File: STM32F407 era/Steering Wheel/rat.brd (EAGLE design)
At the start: 99.2 x 116.2 mm, 117 parts, among them IC1 REG1117, IC3 PCA82C250T, Q1 8 MHz, U2 MAX6817EUT+T, U3 MAX6817EUT+T, U4 MAX6817EUT+T, X1 MINI-USB-SCHIELD-32005-201

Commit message: minor changes
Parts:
- X1: value MINI-USB-SCHIELD-32005-201 -> (none)
- moved C1 5.13 mm to (249.7, -1.29), turned to 90 degrees
- moved Q1 0.95 mm to (249.7, 6.39)
- moved C2 0.88 mm to (249.7, 14.1), turned to 270 degrees
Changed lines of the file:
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@@
 <setting verticaltext="up"/>
 </settings>
-<grid distance="0.0125" unitdist="inch" unit="inch" style="lines" multiple="1" display="yes" altdistance="0.025" altunitdist="inch" altunit="inch"/>
+<grid distance="0.00125" unitdist="inch" unit="inch" style="lines" multiple="1" display="yes" altdistance="0.025" altunitdist="inch" altunit="inch"/>
 <layers>
 <layer number="1" name="Top" color="4" fill="1" visible="yes" active="yes"/>
@@
 </autorouter>
 <elements>
-<element name="Q1" library="crystal" package="HC49U70" value="8 MHz" x="249.659596875" y="7.3434375" rot="R270">
-<attribute name="OC_NEWARK" value="unknown" x="249.659596875" y="7.3434375" size="1.778" layer="27" rot="R270" display="off"/>
-<attribute name="MPN" value="" x="249.659596875" y="7.3434375" size="1.778" layer="27" rot="R270" display="off"/>
-<attribute name="MF" value="" x="249.659596875" y="7.3434375" size="1.778" layer="27" rot="R270" display="off"/>
-<attribute name="OC_FARNELL" value="unknown" x="249.659596875" y="7.3434375" size="1.778" layer="27" rot="R270" display="off"/>
+<element name="Q1" library="crystal" package="HC49U70" value="8 MHz" x="249.659596875" y="6.3909375" rot="R270">
+<attribute name="OC_NEWARK" value="unknown" x="249.659596875" y="6.3909375" size="1.778" layer="27" rot="R270" display="off"/>
+<attribute name="MPN" value="" x="249.659596875" y="6.3909375" size="1.778" layer="27" rot="R270" display="off"/>
+<attribute name="MF" value="" x="249.659596875" y="6.3909375" size="1.778" layer="27" rot="R270" display="off"/>
+<attribute name="OC_FARNELL" value="unknown" x="249.659596875" y="6.3909375" size="1.778" layer="27" rot="R270" display="off"/>
 </element>
 <element name="IC3" library="micro-philips" package="SO8" value="PCA82C250T" x="196.56425" y="20.574" rot="R90">
@@
 <element name="8-BIT-DIP" library="smd-special" package="SMS-008" value="SWS008" x="241.935" y="-13.335" rot="MR0"/>
 <element name="U$5" library="red_segment" package="BIGSEVENSEGMENT" value="BIGSEVENSEGMENT" x="221.615" y="53.975"/>
-<element name="C1" library="rcl" package="C0603K" value="22pf" x="245.535709375" y="1.763078125"/>
-<element name="C2" library="rcl" package="C0603K" value="22pf" x="248.793671875" y="14.207171875"/>
+<element name="C1" library="rcl" package="C0603K" value="22pf" x="249.665171875" y="-1.288790625" rot="R90"/>
+<element name="C2" library="rcl" package="C0603K" value="22pf" x="249.665171875" y="14.064578125" rot="R270"/>
 <element name="R21" library="rcl" package="R0603" value="200" x="233.045" y="-9.2075" rot="R270"/>
 <element name="R22" library="rcl" package="R0603" value="200" x="235.585" y="-9.2075" rot="R270"/>
@@
 <element name="C24" library="microbuilder" package="_0402MP" value="1u" x="245.0465" y="9.81075"/>
 <element name="C25" library="microbuilder" package="_0402MP" value="4u7" x="245.6815" y="4.699"/>
-<element name="X1" library="con-cypressindustries" package="32005-201" value="MINI-USB-SCHIELD-32005-201" x="182.02275" y="-0.0635" rot="R15">
+<element name="X1" library="con-cypressindustries" package="32005-201" value="" x="182.02275" y="-0.0635" rot="R15">
 <attribute name="OC_NEWARK" value="unknown" x="182.02275" y="-0.0635" size="1.778" layer="27" rot="R15" display="off"/>
 <attribute name="MPN" value="" x="182.02275" y="-0.0635" size="1.778" layer="27" rot="R15" display="off"/>
@@
 <contactref element="C2" pad="2"/>
 <contactref element="U1" pad="13"/>
-<wire x1="242.89925" y1="6.57225" x2="246.475409375" y2="6.57225" width="0.3048" layer="1"/>
-<wire x1="246.475409375" y1="6.57225" x2="249.659596875" y2="9.7564375" width="0.3048" layer="1"/>
-<wire x1="249.659596875" y1="9.7564375" x2="249.668671875" y2="9.7655125" width="0.3048" layer="1"/>
-<wire x1="249.668671875" y1="9.7655125" x2="249.668671875" y2="14.207171875" width="0.3048" layer="1"/>
+<wire x1="242.89925" y1="6.57225" x2="247.427909375" y2="6.57225" width="0.3048" layer="1"/>
+<wire x1="247.427909375" y1="6.57225" x2="249.659596875" y2="8.8039375" width="0.3048" layer="1"/>
+<wire x1="249.659596875" y1="8.8039375" x2="249.665171875" y2="8.8095125" width="0.3048" layer="1"/>
+<wire x1="249.665171875" y1="8.8095125" x2="249.665171875" y2="13.189578125" width="0.3048" layer="1"/>
 </signal>
 <signal name="N$2">
@@
 <contactref element="C1" pad="2"/>
 <contactref element="U1" pad="12"/>
-<wire x1="242.89925" y1="6.07225" x2="248.517784375" y2="6.07225" width="0.3048" layer="1"/>
-<wire x1="248.517784375" y1="6.07225" x2="249.659596875" y2="4.9304375" width="0.3048" layer="1"/>
-<wire x1="249.659596875" y1="4.9304375" x2="249.649209375" y2="4.92005" width="0.3048" layer="1"/>
-<wire x1="246.410709375" y1="1.763078125" x2="246.8097375" y2="2.080578125" width="0.3048" layer="1"/>
-<wire x1="246.8097375" y1="2.080578125" x2="249.659596875" y2="4.9304375" width="0.3048" layer="1"/>
+<wire x1="242.89925" y1="6.07225" x2="247.565284375" y2="6.07225" width="0.3048" layer="1"/>
+<wire x1="247.565284375" y1="6.07225" x2="249.659596875" y2="3.9779375" width="0.3048" layer="1"/>
+<wire x1="249.659596875" y1="3.9779375" x2="249.665171875" y2="3.9723625" width="0.3048" layer="1"/>
+<wire x1="249.665171875" y1="3.9723625" x2="249.665171875" y2="-0.413790625" width="0.3048" layer="1"/>
 </signal>
 <signal name="N$51">
@@
 <wire x1="225.17825" y1="1.07225" x2="225.171" y2="1.0795" width="0.3048" layer="1"/>
 <wire x1="225.171" y1="1.0795" x2="225.171" y2="1.651" width="0.3048" layer="1"/>
-<wire x1="248.832" y1="-2.46925" x2="248.82475" y2="-2.4765" width="0.3048" layer="1"/>
 <wire x1="242.89925" y1="10.07225" x2="242.89925" y2="10.06475" width="0.3048" layer="1"/>
 <wire x1="242.89925" y1="10.06475" x2="241.45875" y2="10.06475" width="0.3048" layer="1"/>
@@
 <wire x1="242.89925" y1="5.07225" x2="244.37975" y2="5.07225" width="0.3048" layer="1"/>
 <wire x1="244.37975" y1="5.07225" x2="244.37975" y2="4.73075" width="0.3048" layer="1"/>
-<wire x1="240.79925" y1="14.17225" x2="240.79925" y2="15.12025" width="0.3048" layer="1"/>
-<wire x1="240.79925" y1="15.12025" x2="241.1095" y2="15.4305" width="0.3048" layer="1"/>
-<wire x1="241.1095" y1="15.4305" x2="241.3635" y2="15.4305" width="0.3048" layer="1"/>
-<wire x1="241.3635" y1="15.4305" x2="241.39525" y2="15.46225" width="0.3048" layer="1"/>
-<wire x1="241.39525" y1="15.46225" x2="241.39525" y2="16.16075" width="0.3048" layer="1"/>
-<wire x1="241.39525" y1="16.16075" x2="241.427" y2="16.0655" width="0.3048" layer="1"/>
 <wire x1="244.2178" y1="-14.87" x2="243.16225" y2="-14.87" width="0.3048" layer="1"/>
 <wire x1="243.16225" y1="-14.87" x2="243.078" y2="-14.95425" width="0.3048" layer="1"/>
@@
 <via x="229.39375" y="9.8425" extent="1-16" drill="0.3302"/>
 <via x="229.33025" y="11.684" extent="1-16" drill="0.3302"/>
-<via x="249.39625" y="0.762" extent="1-16" drill="0.3302"/>
+<via x="247.17375" y="-0.1905" extent="1-16" drill="0.3302"/>
 <via x="251.42825" y="13.2715" extent="1-16" drill="0.3302"/>
 <via x="239.903" y="24.28875" extent="1-16" drill="0.3302"/>
@@
 <via x="256.0955" y="23.01875" extent="1-16" drill="0.3302"/>
 <via x="256.0955" y="25.55875" extent="1-16" drill="0.3302"/>
+<wire x1="240.79925" y1="14.17225" x2="240.79925" y2="12.7245" width="0.3048" layer="1"/>
+<wire x1="240.79925" y1="12.7245" x2="241.2365" y2="12.28725" width="0.3048" layer="1"/>
 </signal>
 <signal name="TCTEMPOFF">
@@
 <contactref element="U1" pad="19"/>
 <contactref element="C10" pad="1"/>
-<wire x1="243.79275" y1="9.57225" x2="244.221" y2="9.144" width="0.3048" layer="1"/>
-<wire x1="244.221" y1="9.144" x2="244.5385" y2="9.144" width="0.3048" layer="1"/>
 <contactref element="U1" pad="28"/>
 <contactref element="C9" pad="1"/>
@@
 <wire x1="240.29925" y1="9.57225" x2="240.29925" y2="12.41425" width="0.3048" layer="1"/>
 <wire x1="242.89925" y1="9.57225" x2="240.29925" y2="9.57225" width="0.3048" layer="1"/>
-<wire x1="242.89925" y1="9.57225" x2="243.79275" y2="9.57225" width="0.3048" layer="1"/>
 <wire x1="192.024" y1="9.2075" x2="190.77175" y2="9.2075" width="0.6096" layer="1"/>
 <wire x1="190.77175" y1="9.2075" x2="190.77175" y2="12.573" width="0.6096" layer="1"/>
@@
 <wire x1="252.095" y1="-5.207" x2="254.635" y2="-5.207" width="0.3048" layer="1"/>
 <wire x1="254.635" y1="-5.207" x2="257.7465" y2="-2.0955" width="0.3048" layer="1"/>
+<wire x1="242.89925" y1="9.57225" x2="244.5385" y2="9.57225" width="0.3048" layer="1"/>
+<wire x1="244.5385" y1="9.57225" x2="244.5385" y2="9.81075" width="0.3048" layer="1"/>
 </signal>
 <signal name="12V">
@@
 <via x="229.13975" y="-2.3495" extent="1-16" drill="0.3302"/>
 <wire x1="229.13975" y1="-2.3495" x2="230.124" y2="-3.33375" width="0.3048" layer="16"/>
-<wire x1="247.68175" y1="-3.58775" x2="253.5555" y2="2.286" width="0.3048" layer="16"/>
 <via x="254.92075" y="11.65225" extent="1-16" drill="0.3302"/>
 <wire x1="254.92075" y1="11.65225" x2="257.7465" y2="11.65225" width="0.3048" layer="1"/>
@@
 <wire x1="253.5555" y1="2.286" x2="253.5555" y2="10.287" width="0.3048" layer="16"/>
 <wire x1="253.5555" y1="10.287" x2="254.92075" y2="11.65225" width="0.3048" layer="16"/>
+<wire x1="247.68175" y1="-3.58775" x2="253.5555" y2="2.286" width="0.3048" layer="16"/>
 </signal>
 <signal name="JTAG-TDO">
@@
 </signal>
 </signals>
+<errors>
+</errors>
 </board>
 </drawing>

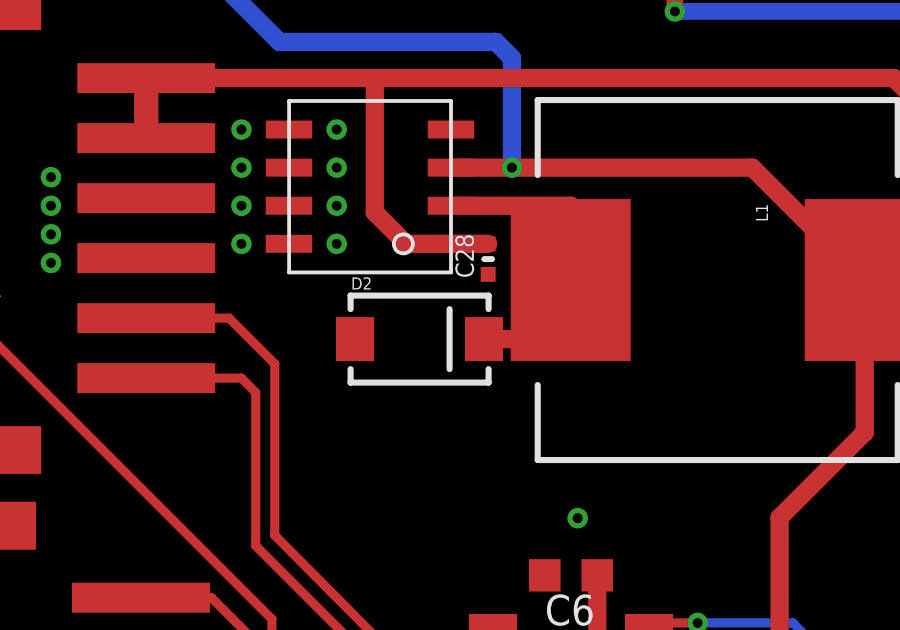
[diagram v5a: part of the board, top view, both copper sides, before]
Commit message: added bracing PCB for rotational switch
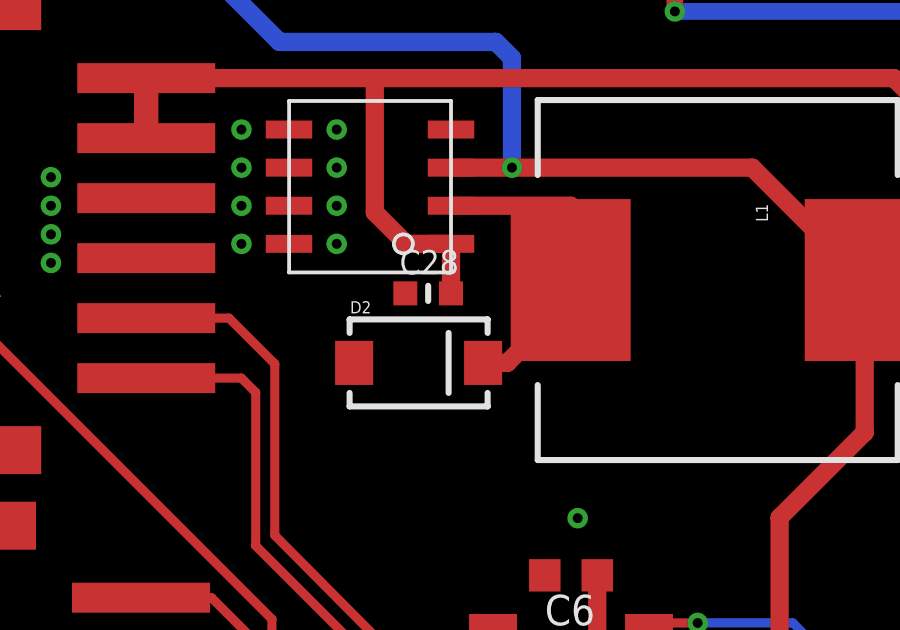
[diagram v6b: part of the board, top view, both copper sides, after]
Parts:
- C28: device microbuilder:_0402MP -> microbuilder:_0603MP
- moved C28 2.30 mm to (191.8, 33.5), turned to 0 degrees
- moved D2 0.79 mm to (191.5, 31.1)
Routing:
- net N$46: track 10.9 -> 11.8 mm
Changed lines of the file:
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@@
 <attribute name="OC_FARNELL" value="unknown" x="182.02275" y="-0.0635" size="1.778" layer="27" rot="R15" display="off"/>
 </element>
-<element name="C28" library="microbuilder" package="_0402MP" value="100n" x="193.802" y="34.6075" rot="R90"/>
+<element name="C28" library="microbuilder" package="_0603MP" value="100n" x="191.80175" y="33.4645"/>
 <element name="L1" library="SparkFun-Passives" package="CDRH125" value="MSS1038-473MLC 47u" x="201.45375" y="33.909" rot="R270"/>
-<element name="D2" library="SparkFun-DiscreteSemi" package="SMA-DIODE" value="B340A-13-F" x="191.516" y="31.9405">
-<attribute name="PROD_ID" value="DIO-08053" x="191.516" y="31.9405" size="1.778" layer="27" display="off"/>
+<element name="D2" library="SparkFun-DiscreteSemi" package="SMA-DIODE" value="B340A-13-F" x="191.48425" y="31.14675">
+<attribute name="PROD_ID" value="DIO-08053" x="191.48425" y="31.14675" size="1.778" layer="27" display="off"/>
 </element>
 <element name="C29" library="microbuilder" package="0805" value="10u" x="210.15325" y="34.0995" rot="R90"/>
@@
 <wire x1="190.02375" y1="36.16325" x2="190.02375" y2="40.64" width="0.6096" layer="1"/>
 <wire x1="182.40525" y1="38.63975" x2="182.405" y2="38.64" width="0.6096" layer="1"/>
-<wire x1="192.56375" y1="35.1155" x2="193.802" y2="35.1155" width="0.6096" layer="1"/>
+<wire x1="192.56375" y1="35.1155" x2="192.56375" y2="33.4645" width="0.6096" layer="1"/>
 <contactref element="IC1" pad="3"/>
 <wire x1="212.3186" y1="39.71925" x2="212.3186" y2="39.9796" width="0.4064" layer="1"/>
@@
 <wire x1="196.55375" y1="36.3855" x2="196.55375" y2="33.909" width="0.6096" layer="1"/>
 <contactref element="D2" pad="C"/>
-<wire x1="193.666" y1="31.9405" x2="195.86575" y2="31.9405" width="0.6096" layer="1"/>
 <wire x1="195.86575" y1="31.9405" x2="196.05625" y2="32.131" width="0.6096" layer="1"/>
-<wire x1="196.05625" y1="32.131" x2="196.05625" y2="33.4115" width="0.6096" layer="1"/>
+<wire x1="196.05625" y1="32.131" x2="196.05625" y2="32.766" width="0.6096" layer="1"/>
+<wire x1="196.05625" y1="32.766" x2="196.05625" y2="33.4115" width="0.6096" layer="1"/>
 <wire x1="196.05625" y1="33.4115" x2="196.55375" y2="33.909" width="0.6096" layer="1"/>
+<wire x1="193.63425" y1="31.14675" x2="194.437" y2="31.14675" width="0.6096" layer="1"/>
+<wire x1="194.437" y1="31.14675" x2="196.05625" y2="32.766" width="0.6096" layer="1"/>
 </signal>
 <signal name="5.0V">
@@
 </signal>
 </signals>
-<errors>
-</errors>
 </board>
 </drawing>

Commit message: continued work on processor board
started doing the layout for the board and startet to add the
interfacing pin rows.
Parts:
- Q1: value 8 MHz -> 25 MHz
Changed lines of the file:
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@@
 </autorouter>
 <elements>
-<element name="Q1" library="crystal" package="HC49U70" value="8 MHz" x="249.659596875" y="6.3909375" rot="R270">
+<element name="Q1" library="crystal" package="HC49U70" value="25 MHz" x="249.659596875" y="6.3909375" rot="R270">
 <attribute name="OC_NEWARK" value="unknown" x="249.659596875" y="6.3909375" size="1.778" layer="27" rot="R270" display="off"/>
 <attribute name="MPN" value="" x="249.659596875" y="6.3909375" size="1.778" layer="27" rot="R270" display="off"/>

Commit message: silkscreen and layout cleanu
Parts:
- renumbered BLUE1 to LED16, BLUE2 to LED15, BLUE3 to LED14, BLUE4 to LED13, BLUE5 to LED12, GREEN1 to LED26, GREEN2 to LED25, GREEN3 to LED24, GREEN4 to LED23, GREEN5 to LED22, LCL to LED27, RED to LED21, RED2 to LED20, RED3 to LED19, RED4 to LED18, RED5 to LED17
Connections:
- removed net N$31: R5.1, S2.P$1, U1.14
- net RESET: now also R5.1, S2.P$1, U1.14
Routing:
- net RESET: track 0.00 -> 69.6 mm, vias 0 -> 2
- net N$31: track 45.9 -> 0.00 mm, vias 2 -> 0
- net 3.3V: track 553.3 -> 555.4 mm, vias 14 -> 13
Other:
- board text removed: "ICSP"
